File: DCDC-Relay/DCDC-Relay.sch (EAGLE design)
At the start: 7 parts, among them J1 1X2-3.5MM, J2 1X2-3.5MM, K2 CMX60D5, U5 TSR 1-2450

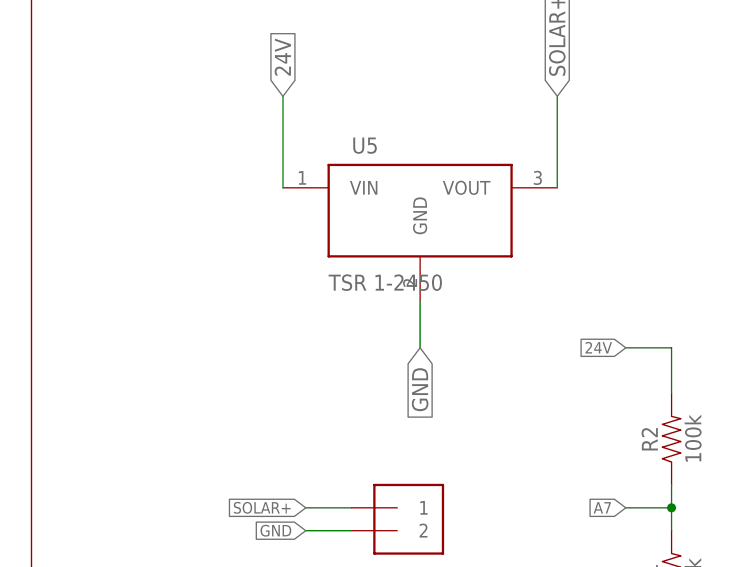
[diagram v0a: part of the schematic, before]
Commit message: Wheatstone ordered
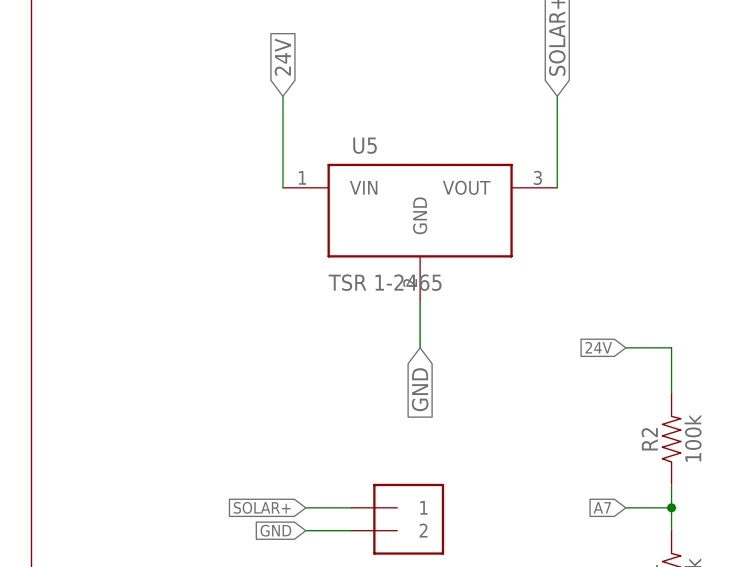
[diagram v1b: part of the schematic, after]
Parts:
- U5: value TSR 1-2450 -> TSR 1-2465
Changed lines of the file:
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@@
 <parts>
 <part name="U$1" library="UIO-John" deviceset="WASPMOTE_V1.5" device=""/>
-<part name="U5" library="DC-DC Converter" deviceset="173010535" device="" package3d_urn="urn:adsk.eagle:package:20779907/3" value="TSR 1-2450"/>
+<part name="U5" library="DC-DC Converter" deviceset="173010535" device="" package3d_urn="urn:adsk.eagle:package:20779907/3" value="TSR 1-2465"/>
 <part name="J2" library="adafruit" library_urn="urn:adsk.eagle:library:420" deviceset="1X2" device="-3.5MM" package3d_urn="urn:adsk.eagle:package:6240635/1"/>
 <part name="J1" library="adafruit" library_urn="urn:adsk.eagle:library:420" deviceset="1X2" device="-3.5MM" package3d_urn="urn:adsk.eagle:package:6240635/1"/>
